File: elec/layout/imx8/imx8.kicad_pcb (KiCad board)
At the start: 2 copper layers, 40 x 40 mm, 0 parts

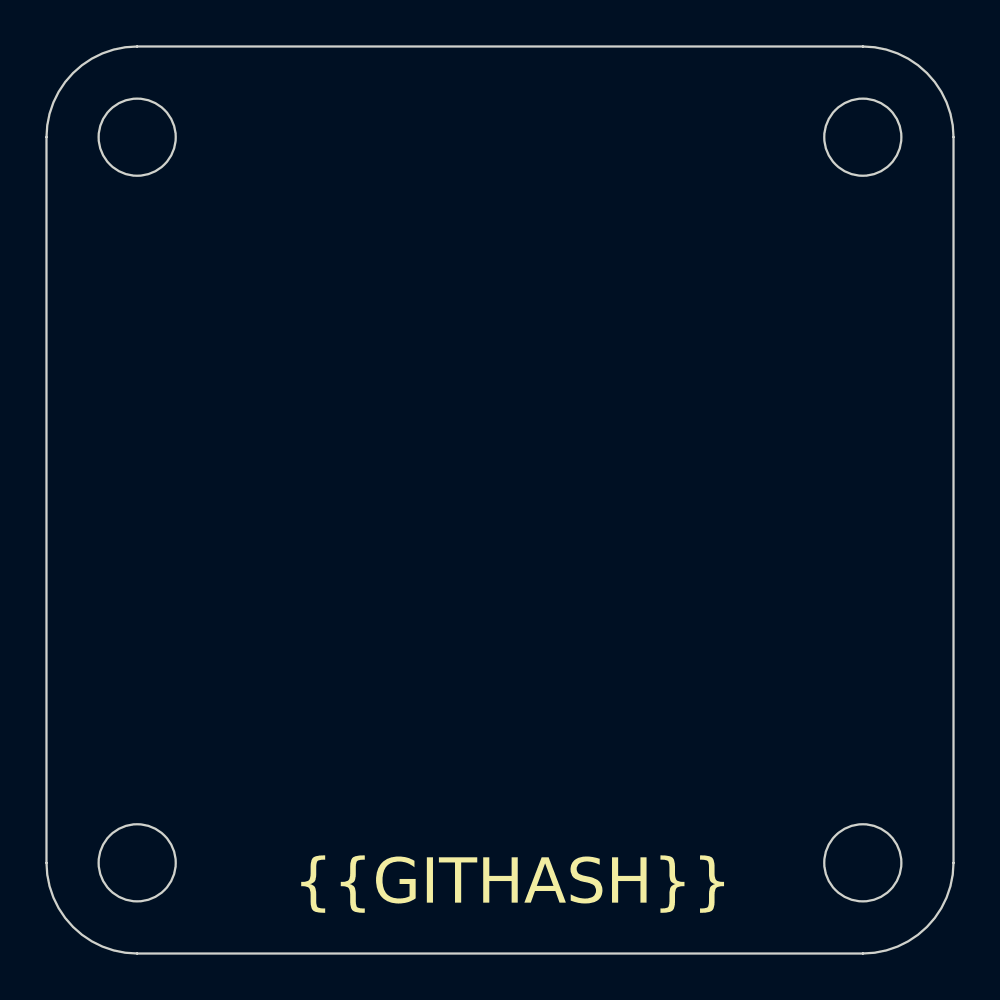
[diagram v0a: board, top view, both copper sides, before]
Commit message: Moved PMIC to this branch, 80% completed power rails for IMX8
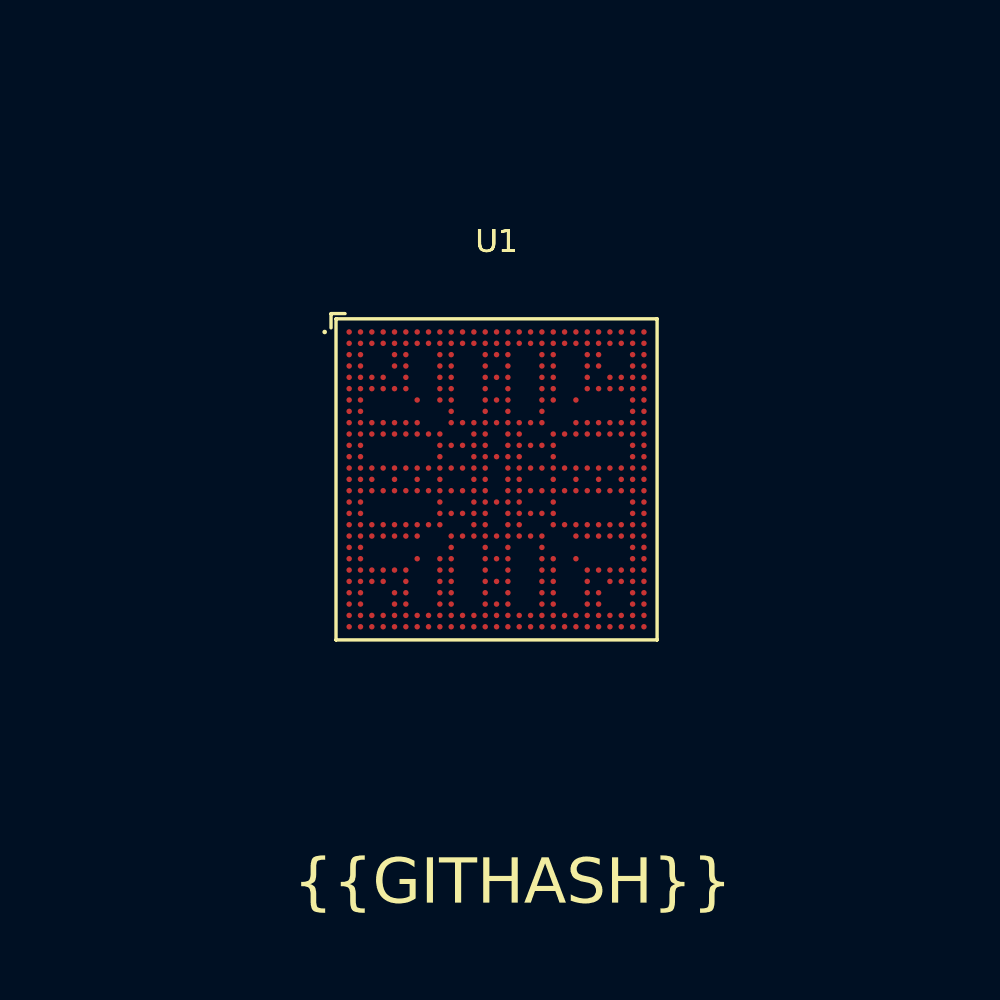
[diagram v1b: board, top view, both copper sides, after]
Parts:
- added U1: _NXP_Semicon_MIMX8MM6CVTKZAA, lcsc:BGA-486_L14.0-W14.0-P0.50-TL_NXP_MIMX8MMXDVTLZXA, F.Cu at (149.2, 97.2)
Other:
- board outline removed

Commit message: Build errors
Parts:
- moved U1 4.84 mm to (148.6, 102.0)
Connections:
- net *BC08.processor-net-0 renamed *BED8.processor-net-2
- net *BC08.processor-net-1 renamed *BED8.processor-net-5
- net *BC08.processor-net-2 renamed *BED8.processor-net-3
- net *BC08.processor-net-3 renamed *BED8.processor-net-8
- net *BC08.processor-net-4 renamed *BED8.processor-net-7
- net *BC08.processor-net-5 renamed *BED8.processor-net-0
- net *BC08.processor-net-6 renamed *BED8.processor-net-1
- net *BC08.processor-net-7 renamed *BED8.processor-net-6
- net *BC08.processor-net-8 renamed *BED8.processor-net-4
- net *BC08.processor-net-9 renamed *BED8.processor-net-9
- net nvcc__enet renamed nvcc_enet

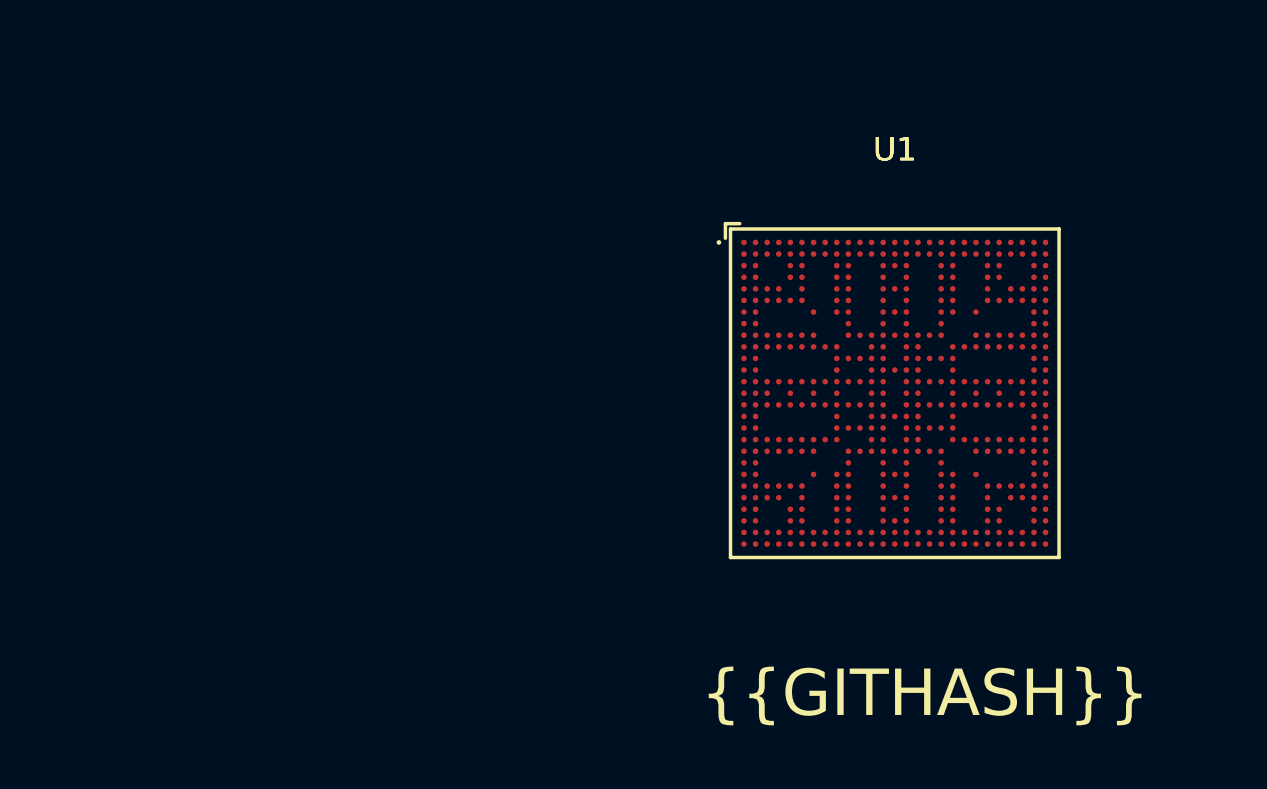
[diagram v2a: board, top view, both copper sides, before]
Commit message: Placed capacitors for IMX8 power
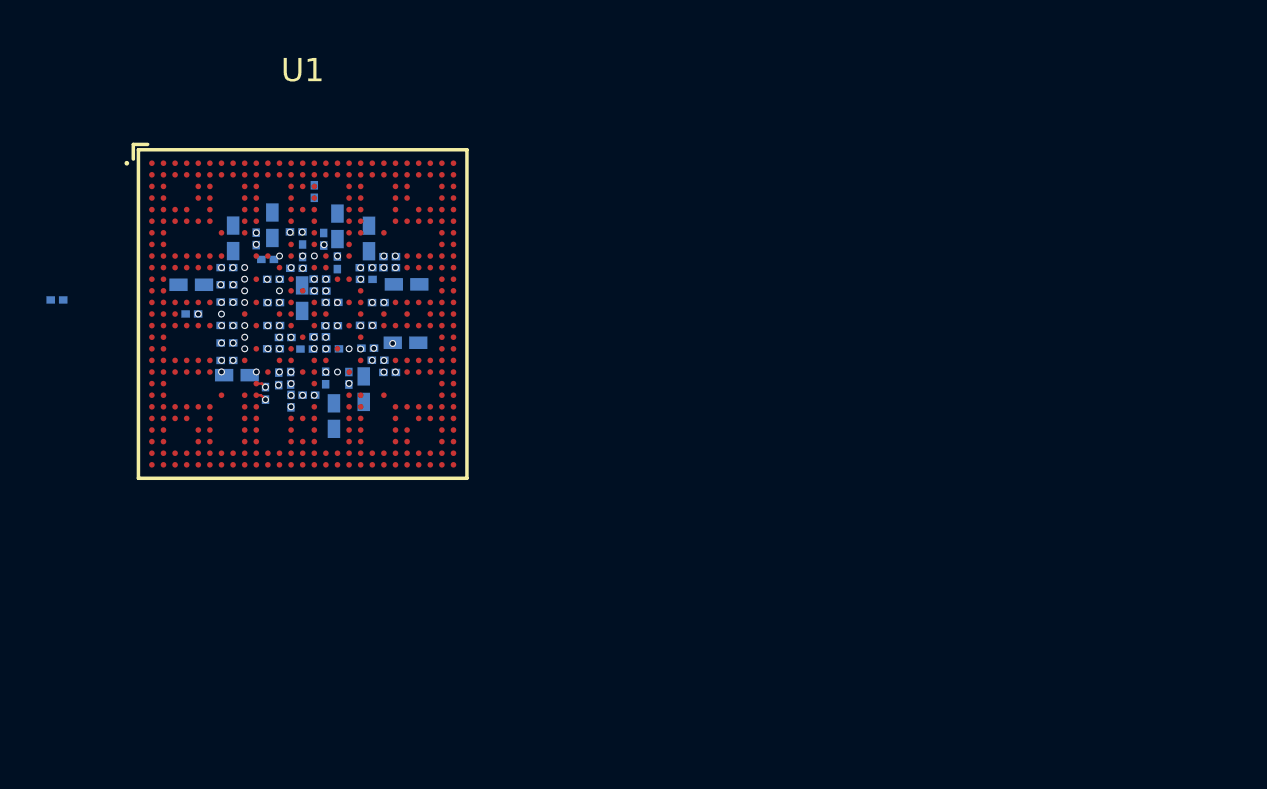
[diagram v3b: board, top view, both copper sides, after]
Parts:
- added C1: 2.2µF ±20% 6.3V X5R, lcsc:C0201, B.Cu at (123.6, 93.3)
- added C10: 220nF ±20% 6.3V X5R, lcsc:C0201, B.Cu at (126.8, 101.1)
- added C11: 220nF ±20% 6.3V X5R, lcsc:C0201, B.Cu at (112.5, 98.0)
- added C12: 1µF ±20% 6.3V X5R, lcsc:C0201, B.Cu at (126.8, 96.1)
- added C13: 220nF ±20% 6.3V X5R, lcsc:C0201, B.Cu at (121.6, 96.2)
- added C14: 1µF ±20% 6.3V X5R, lcsc:C0201, B.Cu at (123.3, 102.1)
- added C15: 10µF ±20% 6.3V X5R, lcsc:C0402, B.Cu at (127.6, 97.3)
- added C16: 220nF ±20% 6.3V X5R, lcsc:C0201, B.Cu at (122.6, 102.3)
- added C17: 10µF ±20% 6.3V X5R, lcsc:C0402, B.Cu at (127.5, 99.8)
- added C18: 220nF ±20% 6.3V X5R, lcsc:C0201, B.Cu at (125.9, 100.1)
- added C19: 220nF ±20% 6.3V X5R, lcsc:C0201, B.Cu at (126.3, 98.1)
- added C2: 10µF ±20% 6.3V X5R, lcsc:C0402, B.Cu at (120.1, 95.3)
- added C20: 220nF ±20% 6.3V X5R, lcsc:C0201, B.Cu at (125.8, 99.1)
- added C21: 220nF ±20% 6.3V X5R, lcsc:C0201, B.Cu at (126.3, 100.6)
- added C22: 220nF ±20% 6.3V X5R, lcsc:C0201, B.Cu at (122.8, 95.0)
- added C23: 220nF ±20% 6.3V X5R, lcsc:C0201, B.Cu at (125.8, 97.1)
- added C24: 220nF ±20% 6.3V X5R, lcsc:C0201, B.Cu at (122.0, 101.4)
- added C25: 4.7µF ±20% 10V X5R, lcsc:C0402, B.Cu at (124.4, 103.0)
- added C26: 220nF ±20% 6.3V X5R, lcsc:C0201, B.Cu at (125.8, 96.6)
- added C27: 220nF ±20% 6.3V X5R, lcsc:C0201, B.Cu at (125.1, 101.4)
- added C28: 220nF ±20% 6.3V X5R, lcsc:C0201, B.Cu at (121.5, 102.0)
- added C29: 220nF ±20% 6.3V X5R, lcsc:C0201, B.Cu at (121.1, 95.3)
- added C3: 10µF ±20% 6.3V X5R, lcsc:C0402, B.Cu at (118.3, 97.3)
- added C30: 10µF ±20% 6.3V X5R, lcsc:C0402, B.Cu at (125.7, 101.8)
- added C31: 1µF ±20% 6.3V X5R, lcsc:C0201, B.Cu at (123.3, 100.1)
- added C32: 1µF ±20% 6.3V X5R, lcsc:C0201, B.Cu at (124.1, 101.3)
- added C33: 1µF ±20% 6.3V X5R, lcsc:C0201, B.Cu at (123.8, 99.6)
- added C34: 1µF ±20% 6.3V X5R, lcsc:C0201, B.Cu at (122.3, 99.6)
- added C35: 1µF ±20% 6.3V X5R, lcsc:C0201, B.Cu at (122.6, 101.4)
- added C36: 10µF ±20% 6.3V X5R, lcsc:C0402, B.Cu at (120.2, 101.2)
- added C37: 10µF ±20% 6.3V X5R, lcsc:C0402, B.Cu at (121.8, 94.8)
- added C38: 1µF ±20% 6.3V X5R, lcsc:C0201, B.Cu at (118.3, 98.6)
- added C39: 1µF ±20% 6.3V X5R, lcsc:C0201, B.Cu at (121.8, 100.1)
- added C4: 1µF ±20% 6.3V X5R, lcsc:C0201, B.Cu at (119.8, 96.6)
- added C40: 1µF ±20% 6.3V X5R, lcsc:C0201, B.Cu at (121.8, 98.1)
- added C41: 1µF ±20% 6.3V X5R, lcsc:C0201, B.Cu at (122.8, 96.6)
- added C42: 1µF ±20% 6.3V X5R, lcsc:C0201, B.Cu at (121.8, 97.1)
- added C43: 1µF ±20% 6.3V X5R, lcsc:C0201, B.Cu at (121.8, 99.1)
- added C44: 220nF ±20% 6.3V X5R, lcsc:C0201, B.Cu at (123.1, 95.9)
- added C45: 2.2µF ±20% 6.3V X5R, lcsc:C0402, B.Cu at (124.6, 94.8)
- added C46: 220nF ±20% 6.3V X5R, lcsc:C0201, B.Cu at (124.0, 95.4)
- added C47: 220nF ±20% 6.3V X5R, lcsc:C0201, B.Cu at (126.8, 96.6)
- added C48: 10µF ±20% 6.3V X5R, lcsc:C0402, B.Cu at (123.1, 97.9)
- added C49: 4.7µF ±20% 10V X5R, lcsc:C0402, B.Cu at (125.9, 95.3)
- added C5: 1µF ±20% 6.3V X5R, lcsc:C0201, B.Cu at (119.8, 97.3)
- added C50: 1µF ±20% 6.3V X5R, lcsc:C0201, B.Cu at (123.8, 97.1)
- added C51: 1µF ±20% 6.3V X5R, lcsc:C0201, B.Cu at (123.8, 97.6)
- added C52: 1µF ±20% 6.3V X5R, lcsc:C0201, B.Cu at (124.4, 100.1)
- added C53: 1µF ±20% 6.3V X5R, lcsc:C0201, B.Cu at (124.3, 98.1)
- added C54: 1µF ±20% 6.3V X5R, lcsc:C0201, B.Cu at (124.6, 96.4)
- added C55: 220nF ±20% 6.3V X5R, lcsc:C0201, B.Cu at (124.3, 99.1)
- added C6: 1µF ±20% 6.3V X5R, lcsc:C0201, B.Cu at (119.8, 98.1)
- added C7: 1µF ±20% 6.3V X5R, lcsc:C0201, B.Cu at (119.8, 100.6)
- added C8: 1µF ±20% 6.3V X5R, lcsc:C0201, B.Cu at (119.8, 99.1)
- added C9: 1µF ±20% 6.3V X5R, lcsc:C0201, B.Cu at (119.8, 99.8)
- moved U1 25.7 mm to (123.1, 98.6)
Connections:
- net *BED8.processor-net-0 renamed NVCC_DRAM_1V1
- net *BED8.processor-net-2 renamed GND
- net *BED8.processor-net-3 renamed VDD_ARM_0V9
- U1 pad AA14: *BED8.processor-net-8 -> VDDA_1V8
- U1 pad AB13: pvcc0_1p8 -> VDDA_1V8
- U1 pad D15: mipi_vreg_cap -> *7B78.processor-net-1
- U1 pad G14: vdd_pci_1p8 -> VDDA_1V8
- U1 pad H10: nvcc_escpi -> VDD_3V3
- U1 pad H13: vdd_mipi_1p8 -> VDDA_1V8
- U1 pad H15: vdd_usb_1p8 -> VDDA_1V8
- U1 pad J10: *BED8.processor-net-7 -> VDD_DRAM_0V9
- U1 pad J11: nvcc_i2c -> VDDA_1V8
- U1 pad J12: nvcc_uart -> VDDA_1V8
- U1 pad J13: pvcc2_1p8 -> VDDA_1V8
- U1 pad J14: vdd_mipi_0p9 -> VDD_PHY_0V9
- U1 pad J15: vdd_mipi_1p2 -> VDD_PHY_1V2
- U1 pad J16: vdd_pci_0p8 -> VDD_SOC_0V8
- U1 pad J17: vdd_usb_0p8 -> VDD_SOC_0V8
- U1 pad J22: nvcc_snvs_1p8 -> *7B78.processor-net-0
- U1 pad K12: *BED8.processor-net-1 -> VDD_DRAM_0V9
- U1 pad K13: *BED8.processor-net-1 -> VDD_DRAM_0V9
- U1 pad K15: *BED8.processor-net-5 -> VDD_SOC_0V8
- U1 pad K16: *BED8.processor-net-5 -> VDD_SOC_0V8
- U1 pad K19: vdd_usb_3p3 -> VDD_3V3
- U1 pad K22: vdd_snvs_0p8 -> VDD_SNVS_0V8
- U1 pad L10: *BED8.processor-net-7 -> VDD_DRAM_0V9
- U1 pad L11: *BED8.processor-net-1 -> VDD_DRAM_0V9
- U1 pad L13: *BED8.processor-net-1 -> VDD_DRAM_0V9
- U1 pad L15: *BED8.processor-net-5 -> VDD_SOC_0V8
- U1 pad L17: *BED8.processor-net-9 -> VDD_SOC_0V8
- U1 pad L18: *BED8.processor-net-5 -> VDD_SOC_0V8
- U1 pad L19: nvcc_jtag -> VDDA_1V8
- U1 pad M13: *BED8.processor-net-1 -> VDD_DRAM_0V9
- U1 pad M14: *BED8.processor-net-1 -> VDD_DRAM_0V9
- U1 pad M15: *BED8.processor-net-5 -> VDD_SOC_0V8
- U1 pad M19: nvcc_clk -> VDDA_1V8
- U1 pad N10: *BED8.processor-net-7 -> VDD_DRAM_0V9
- U1 pad N11: *BED8.processor-net-1 -> VDD_DRAM_0V9
- U1 pad N13: *BED8.processor-net-5 -> VDD_SOC_0V8
- U1 pad N15: *BED8.processor-net-5 -> VDD_SOC_0V8
- U1 pad N17: *BED8.processor-net-9 -> VDD_SOC_0V8
- U1 pad N18: *BED8.processor-net-5 -> VDD_SOC_0V8
- U1 pad N19: vdd_24m_xtal_1p8 -> VDDA_1V8
- U1 pad N20: *BED8.processor-net-4 -> VDDA_1V8
- U1 pad P12: *BED8.processor-net-6 -> VDD_DRAM_0V9
- U1 pad P16: vdd_arm_pll_0p8 -> VDD_SOC_0V8
- U1 pad P19: *BED8.processor-net-4 -> VDDA_1V8
- U1 pad P5: vdd_dram_pll_1p8 -> VDD_DRAM_0V9
- U1 pad R10: *BED8.processor-net-7 -> VDD_DRAM_0V9
- U1 pad R11: *BED8.processor-net-6 -> VDD_DRAM_0V9
- U1 pad R17: *BED8.processor-net-5 -> VDD_SOC_0V8
- U1 pad R18: *BED8.processor-net-5 -> VDD_SOC_0V8
- U1 pad R19: vdd_arm_pll_1p8 -> VDDA_1V8
- U1 pad T19: pvcc1_1p8 -> VDDA_1V8
- U1 pad U10: *BED8.processor-net-7 -> VDD_DRAM_0V9
- U1 pad U11: *BED8.processor-net-6 -> VDD_DRAM_0V9
- U1 pad U17: *BED8.processor-net-5 -> VDD_SOC_0V8
- U1 pad U18: *BED8.processor-net-5 -> VDD_SOC_0V8
- U1 pad U19: nvcc_nand -> VDDA_1V8
- U1 pad V12: *BED8.processor-net-6 -> VDD_DRAM_0V9
- U1 pad V19: nvcc_sai2 -> VDDA_1V8
- U1 pad V20: nvcc_sd1 -> VDDA_1V8
- U1 pad W10: *BED8.processor-net-7 -> VDD_DRAM_0V9
- U1 pad W11: *BED8.processor-net-6 -> VDD_DRAM_0V9
- U1 pad W12: nvcc_gpio1 -> VDDA_1V8
- U1 pad W17: nvcc_sai5 -> VDD_3V3
- U1 pad W18: nvcc_sai1 -> VDD_3V3
- U1 pad W22: nvcc_enet -> NVCC_ENET
- U1 pad Y10: nvcc_sai3 -> VDD_3V3
- U1 pad Y15: *BED8.processor-net-8 -> VDDA_1V8
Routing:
- net GND: track 0.00 -> 0.48 mm, vias 0 -> 36
- net VDD_3V3: track 0.00 -> 0.46 mm, vias 0 -> 4
- net VDD_SOC_0V8: track 0.00 -> 0.10 mm, vias 0 -> 6
- net NVCC_DRAM_1V1: track 0.00 -> 0.01 mm, vias 0 -> 14
- net VDD_SNVS_0V8: vias 0 -> 1
- net VDD_PHY_1V2: vias 0 -> 2
- net VDD_PHY_0V9: vias 0 -> 1
- net VDD_DRAM_0V9: vias 0 -> 7
- net VDD_ARM_0V9: vias 0 -> 5
- net VDDA_1V8: vias 0 -> 11
- net NVCC_ENET: vias 0 -> 1
- net *7B78.processor-net-0: vias 0 -> 1
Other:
- board text removed: "{{GITHASH}}"

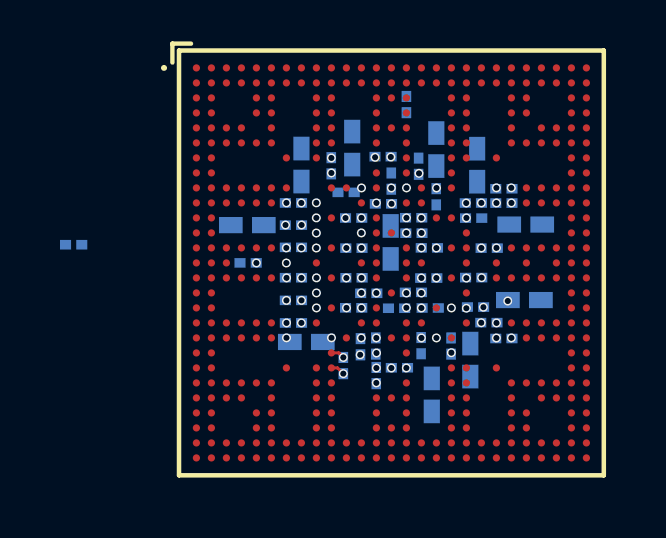
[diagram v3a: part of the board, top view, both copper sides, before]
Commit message: update SD2 cap
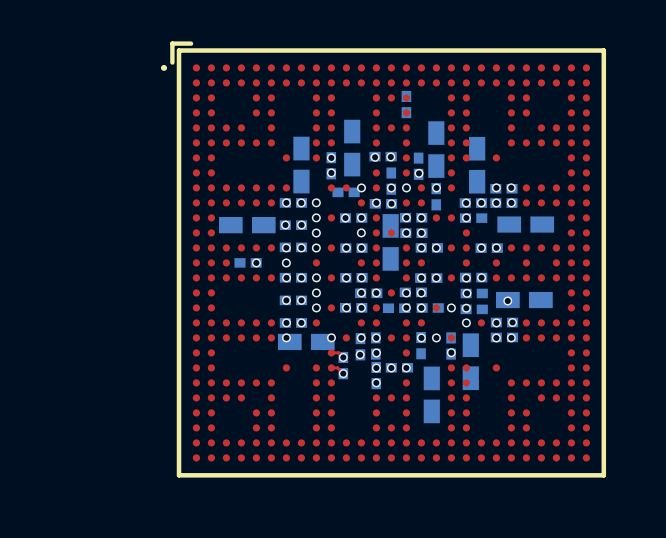
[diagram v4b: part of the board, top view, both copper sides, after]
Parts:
- moved C11 14.6 mm to (126.8, 100.6)
- moved C21 0.66 mm to (125.8, 100.1)
- moved C18 0.45 mm to (125.8, 99.6)
- moved C30 0.06 mm to (125.7, 101.9)
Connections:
- net *7B78.processor-net-0 renamed *7C08.processor-net-1
- net *7B78.processor-net-1 renamed *7C08.processor-net-0
- U1 pad V22: nvcc_sd2 -> NVCC_SD2
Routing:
- net VDDA_1V8: vias 11 -> 12
- net NVCC_SD2: vias 0 -> 1
- net GND: vias 36 -> 35

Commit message: PMIC building! Net short issue figured out in imx8
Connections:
- net *7C08.processor-net-0 renamed *3B78.processor-net-0
- net *7C08.processor-net-1 renamed *3B78.processor-net-1
- C15 pad 1: VDDA_1V8 -> VDD_1V8
- C16 pad 1: VDDA_1V8 -> VDD_1V8
- C17 pad 1: VDDA_1V8 -> VDD_1V8
- C18 pad 1: VDDA_1V8 -> VDD_1V8
- C19 pad 1: VDDA_1V8 -> VDD_1V8
- C20 pad 1: VDDA_1V8 -> VDD_1V8
- C21 pad 1: VDDA_1V8 -> VDD_1V8
- C22 pad 1: VDDA_1V8 -> VDD_1V8
- C23 pad 1: VDDA_1V8 -> VDD_1V8
- C24 pad 1: VDDA_1V8 -> VDD_1V8
- U1 pad AA14: VDDA_1V8 -> VDD_1V8
- U1 pad AB13: VDDA_1V8 -> VDD_1V8
- U1 pad G14: VDDA_1V8 -> VDD_1V8
- U1 pad H13: VDDA_1V8 -> VDD_1V8
- U1 pad H15: VDDA_1V8 -> VDD_1V8
- U1 pad J11: VDDA_1V8 -> VDD_1V8
- U1 pad J12: VDDA_1V8 -> VDD_1V8
- U1 pad J13: VDDA_1V8 -> VDD_1V8
- U1 pad L19: VDDA_1V8 -> VDD_1V8
- U1 pad M19: VDDA_1V8 -> VDD_1V8
- U1 pad N20: VDDA_1V8 -> VDD_1V8
- U1 pad P19: VDDA_1V8 -> VDD_1V8
- U1 pad T19: VDDA_1V8 -> VDD_1V8
- U1 pad U19: VDDA_1V8 -> VDD_1V8
- U1 pad V19: VDDA_1V8 -> VDD_1V8
- U1 pad V20: VDDA_1V8 -> VDD_1V8
- U1 pad W12: VDDA_1V8 -> VDD_1V8
- U1 pad Y15: VDDA_1V8 -> VDD_1V8
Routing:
- net *3B78.processor-net-1: vias 1 -> 0
- net *3B78.processor-net-0: vias 0 -> 1

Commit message: Fixing build errors
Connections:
- net *3B78.processor-net-0 renamed *38A8.processor-net-1
- net *3B78.processor-net-1 renamed *38A8.processor-net-0

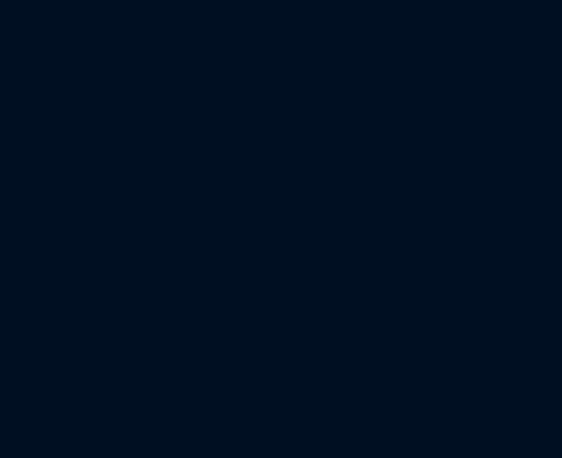
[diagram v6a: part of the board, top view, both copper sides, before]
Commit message: Footprint path problems
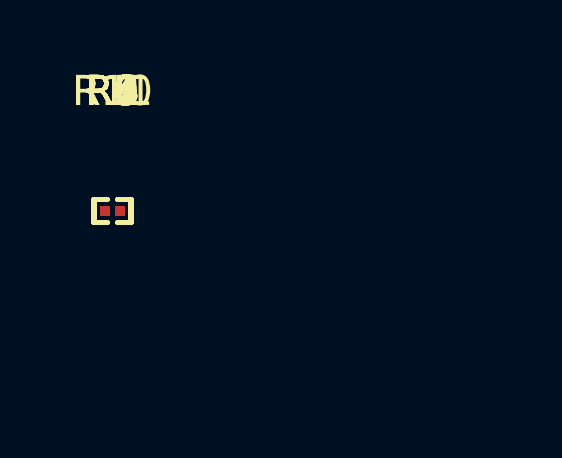
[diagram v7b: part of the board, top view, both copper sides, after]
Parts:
- added R1, R2, R3, R4, R5, R6, R7, R8: 4.87kΩ ±1% 50mW, lcsc:R0201, F.Cu at (0.00, 0.00)
- added R10, R11, R9: 100kΩ ±1% 50mW, lcsc:R0201, F.Cu at (0.00, 0.00)
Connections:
- net *38A8.processor-net-0 renamed *7C08-hv
- net *38A8.processor-net-1 renamed *7C08-net-7
- U1 pad D10: i2c2_scl -> *7C08-net-1
- U1 pad D13: i2c4_scl -> *7C08-net-5
- U1 pad D9: i2c2_sda -> *7C08-net-6
- U1 pad E10: i2c3_scl -> *7C08-net-0
- U1 pad E13: i2c4_sda -> *7C08-net-3
- U1 pad E9: i2c1_scl -> *7C08-net-2
- U1 pad F10: i2c3_sda -> *7C08-net-8
- U1 pad F9: i2c1_sda -> *7C08-net-4
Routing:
- net *7C08-net-7: vias 1 -> 0
- net (no net): vias 0 -> 1

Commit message: add library components
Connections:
- net *7C08-hv renamed *3E48.processor-hv
- net *7C08-net-0 renamed *3E48.processor-net-7
- net *7C08-net-1 renamed *3E48.processor-net-8
- net *7C08-net-2 renamed *3E48.processor-net-3
- net *7C08-net-3 renamed *3E48.processor-net-4
- net *7C08-net-4 renamed *3E48.processor-net-0
- net *7C08-net-5 renamed *3E48.processor-net-1
- net *7C08-net-6 renamed *3E48.processor-net-2
- net *7C08-net-7 renamed *3E48.processor-net-5
- net *7C08-net-8 renamed *3E48.processor-net-6
- net *7C08.I2C1-hv renamed *3E48.processor.I2C1-hv
- net *7C08.I2C2-hv renamed *3E48.processor.I2C2-hv
- net *7C08.I2C3-hv renamed *3E48.processor.I2C3-hv
- net *7C08.I2C4-hv renamed *3E48.processor.I2C4-hv
- net *7C08.ONOFF-signal renamed *3E48.processor.ONOFF-signal
- net *7C08.PMIC_ON_REQ-signal renamed *3E48.processor.PMIC_ON_REQ-signal
- net *7C08.PMIC_STBY_REQ-signal renamed *3E48.processor.PMIC_STBY_REQ-signal
